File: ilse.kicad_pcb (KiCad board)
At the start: 2 copper layers, 80.9 x 128.5 mm, 89 parts, among them J1 OUT, J2 EURO RACK POWER, J3 CV Inputs, J4 1V/Oct, J5 Gate, J6 Cutoff, J7 Filter In, Q1 BC560, Q2 BC560, Q3 BC560, Q4 BC550, Q5 BC550, Q6 BC550, SW1 Power Switch, SW2 LFO to Filter / Freq CV, SW3 Resonance L/H, U1 TL074, U2 TL074

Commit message: incorporates max's powersupply protection
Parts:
- removed SW1: Power Switch, chair:PVA2
- added D3: 1N5819, Diode_THT:D_DO-41_SOD81_P10.16mm_Horizontal, F.Cu at (46.6, 85.0)
- added D4: 1N5819, Diode_THT:D_DO-41_SOD81_P10.16mm_Horizontal, F.Cu at (46.6, 89.3)
- RV7: value 100kA -> 100kB
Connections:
- C12 pad 1: Net-(BT1-Pad1) -> VCC
- C13 pad 2: Net-(BT2-Pad2) -> VSS
- SW2 pad 4: Net-(SW2-Pad4) -> unconnected-(SW2-Pad4)
- SW3 pad 3: Net-(SW3-Pad3) -> unconnected-(SW3-Pad3)

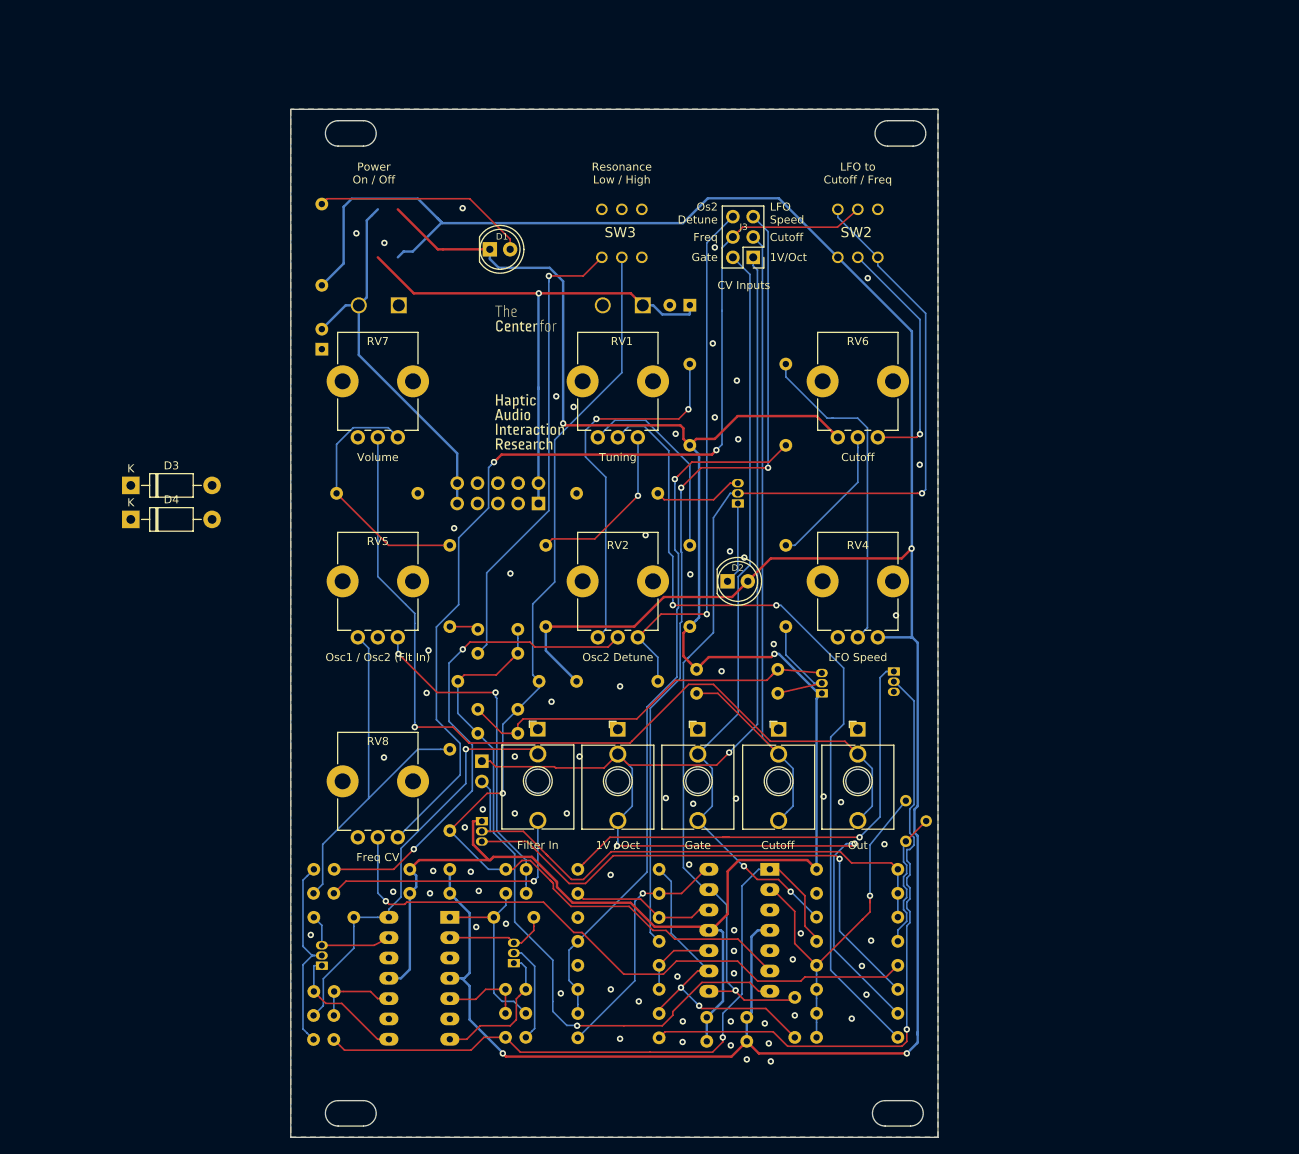
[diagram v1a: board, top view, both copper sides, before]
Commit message: added hybrid lib
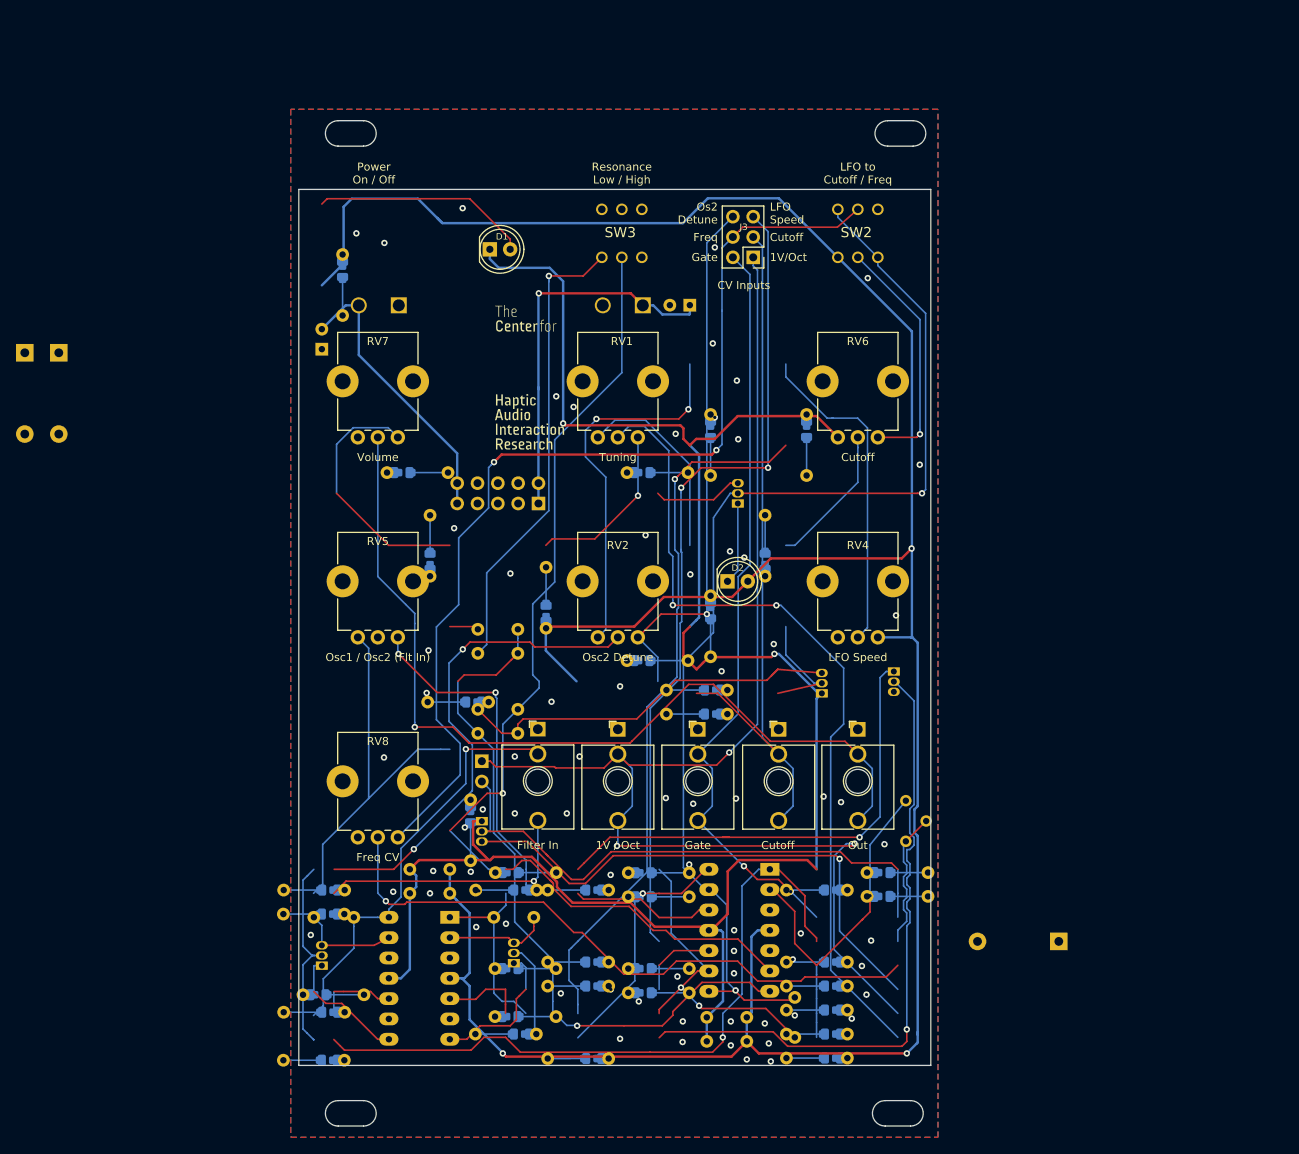
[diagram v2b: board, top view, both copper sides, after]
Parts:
- added D5: 1N5819, Diode_THT:D_DO-41_SOD81_P10.16mm_Horizontal, B.Cu at (162.6, 142.0)
- C8, C9: value 22n -> 47n
- D3, D4: moved to B.Cu
- R1, R12, R15, R19, R2, R20, R21, R23, R27, R28, R29, R3, R30, R31, R32, R33, R34, R35, R36, R37, R38, R39, R4, R40, R7, R8, R9: footprint Resistor_THT:R_Axial_DIN0207_L6.3mm_D2.5mm_P10.16mm_Horizontal -> hybrid:R (hybrid SMD-THT)
- R10, R11, R13, R14, R16, R17, R18, R22, R5, R6: footprint Resistor_THT:R_Axial_DIN0207_L6.3mm_D2.5mm_P2.54mm_Vertical -> hybrid:R (hybrid SMD-THT)
- R24, R25: value 47k -> 100k; footprint Resistor_THT:R_Axial_DIN0207_L6.3mm_D2.5mm_P10.16mm_Horizontal -> hybrid:R (hybrid SMD-THT)
- R26: value 100k -> 10k; footprint Resistor_THT:R_Axial_DIN0207_L6.3mm_D2.5mm_P10.16mm_Horizontal -> hybrid:R (hybrid SMD-THT)
- moved D4 24.7 mm to (33.4, 68.4), turned to -90 degrees
- moved D3 18.9 mm to (37.6, 68.4), turned to -90 degrees
- moved R1 7.02 mm to (101.1, 99.0)
- moved R34 0.12 mm to (86.6, 92.5)
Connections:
- Q5 pad 1: VSS -> GND
- R26 pad 1: VSS -> Net-(C8-Pad2)
- R26 pad 2: Net-(C8-Pad2) -> Net-(Q5-Pad2)
- RV6 pad 1: VSS -> GND
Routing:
- net VSS: track 271.1 -> 843.9 mm, vias 3 -> 11
- net VCC: track 351.4 -> 704.1 mm, vias 3 -> 10
- net 1V/Oct: track 165.8 -> 0.00 mm, vias 3 -> 0
- net Net-(C7-Pad2): track 143.7 -> 0.00 mm, vias 2 -> 0
- net Net-(Q5-Pad2): track 15.1 -> 125.9 mm, vias 0 -> 1
- net Net-(J1-PadT): track 110.8 -> 0.00 mm, vias 1 -> 0
- net LFO Speed: track 103.2 -> 0.00 mm, vias 2 -> 0
- net Net-(R7-Pad2): track 102.6 -> 0.00 mm, vias 2 -> 0
- net Net-(R18-Pad1): track 48.1 -> 143.8 mm, vias 0 -> 3
- net Net-(C8-Pad1): track 131.3 -> 39.9 mm, vias 1 -> 2
- net Net-(R30-Pad1): track 17.9 -> 107.1 mm
- net Filter Cutoff: track 89.2 -> 0.00 mm
- net Net-(R19-Pad1): track 88.7 -> 0.00 mm, vias 1 -> 0
- net Net-(R15-Pad1): track 88.1 -> 0.00 mm
- net Net-(C7-Pad1): track 40.8 -> 117.8 mm, vias 2 -> 3
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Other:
- board size 80.9 x 128.5 mm -> 79 x 109.5 mm

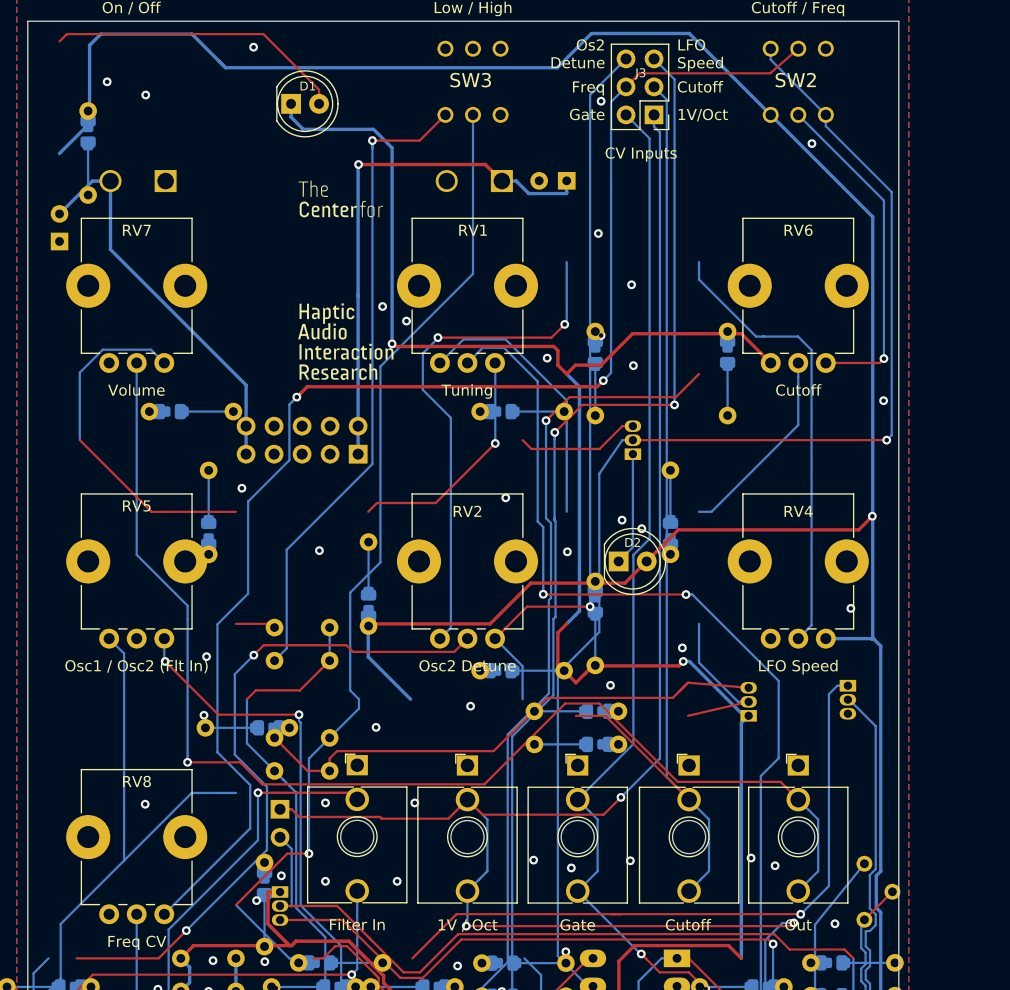
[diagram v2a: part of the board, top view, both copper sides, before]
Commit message: edits in schematic
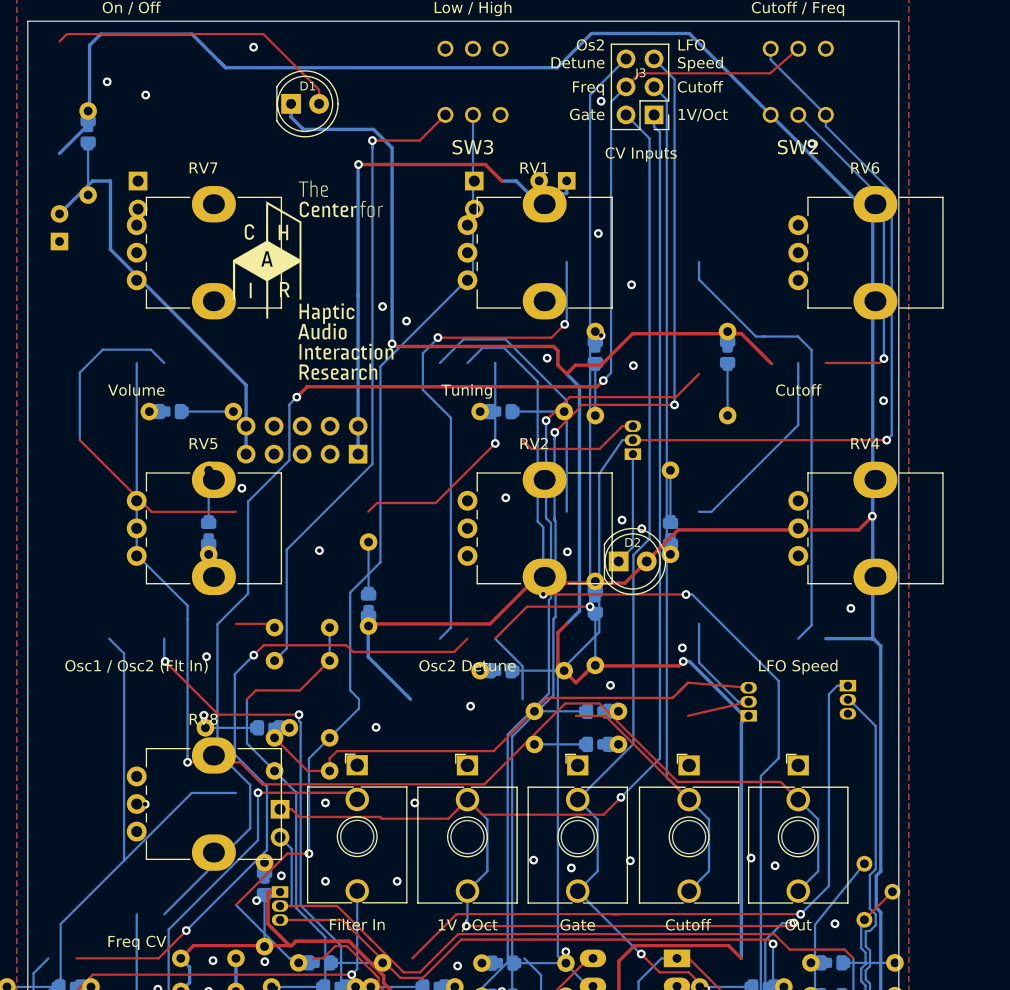
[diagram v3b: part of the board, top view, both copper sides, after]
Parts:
- BT1, BT2: footprint chair:Battery Connector -> Connector_PinHeader_2.54mm:PinHeader_1x02_P2.54mm_Vertical
- J1, J4, J5, J6, J7: footprint chair:Jack_3.5mm_QingPu_WQP-PJ398SM_Vertical_CircularHoles -> CHAIR:Jack_3.5mm_QingPu_WQP-WQP518MA
- J2: footprint 4ms-footprints:Euro_Header_10-pin_TH -> CHAIR:Euro_Header_10-pin_TH
- LOGO1: footprint chair:CHAIR -> CHAIR:CHAIR_logo_silkscreen
- RV1, RV2, RV4, RV5, RV6, RV7, RV8: footprint chair:Potentiometer_Alps_RK09K_Single_Vertical -> CHAIR:Potentiometer_Alps_RK09K_Single_Vertical
- SW2, SW3: footprint chair:PVA2 -> CHAIR:Switch_DPDT_PVA2
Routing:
- net VCC: track 704.1 -> 814.2 mm, vias 10 -> 12
- net Net-(R36-Pad2): track 102.6 -> 0.00 mm, vias 2 -> 1
- net Net-(C8-Pad1): track 39.9 -> 0.00 mm
- net Net-(Q4-Pad1): track 60.8 -> 100.7 mm
- net GND: track 58.9 -> 21.4 mm, vias 66 -> 64
- net GATE: track 95.3 -> 132.8 mm, vias 2 -> 3
- net Net-(R34-Pad1): track 32.0 -> 15.1 mm
- net Net-(Q5-Pad2): track 125.9 -> 142.8 mm
- net Net-(BT1-Pad1): track 47.6 -> 40.1 mm

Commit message: layout remake in process
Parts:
- C1, C10, C11, C2, C3, C4, C5, C6, C7, C8, C9: footprint Capacitor_THT:C_Rect_L7.2mm_W2.5mm_P5.00mm_FKS2_FKP2_MKS2_MKP2 -> hybrid:C_Disc_(hybrid SMD-THT)_P5.00mm-0604
- D3, D4: footprint Diode_THT:D_DO-41_SOD81_P10.16mm_Horizontal -> Diode_THT:D_DO-35_SOD27_P7.62mm_Horizontal
- D5: footprint Diode_THT:D_DO-41_SOD81_P10.16mm_Horizontal -> Diode_THT:D_DO-35_SOD27_P7.62mm_Horizontal; moved to F.Cu
- Q1, Q2, Q3: value BC560 -> BC559
- Q4, Q5, Q6: value BC550 -> BC548
- R7: value 20k -> 22k
- U1, U2: footprint Package_DIP:DIP-14_W7.62mm_Socket_LongPads -> Package_DIP:DIP-14_W7.62mm
- moved D5 105.6 mm to (71.3, 88.9), turned to 0 degrees
- moved D3 92.4 mm to (130.0, 71.5), turned to -135 degrees
- moved D4 92.0 mm to (124.6, 80.6), turned to 45 degrees
- moved R31 78.2 mm to (189.9, 74.8)
- moved C13 65.4 mm to (134.9, 79.3), turned to 135 degrees
- moved R12 60.0 mm to (126.7, 39.0), turned to 180 degrees
- moved BT2 46.2 mm to (121.2, 77.8)
- moved LOGO1 28.1 mm to (117.7, 57.1)
- moved R20 27.3 mm to (137.4, 139.4)
- moved R6 27.3 mm to (94.2, 142.6)
- moved H3 27.3 mm to (167.5, 29.4)
- moved J1 27.3 mm to (162.2, 103.9)
- moved J4 27.3 mm to (132.2, 103.9)
- moved J5 27.3 mm to (142.2, 103.9)
- moved J6 27.3 mm to (152.3, 103.9)
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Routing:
- net VSS: track 843.9 -> 261.7 mm, vias 11 -> 3
- net VCC: track 814.2 -> 301.9 mm, vias 12 -> 8
- net 1V/Oct: track 0.00 -> 425.4 mm, vias 0 -> 7
- net Net-(C7-Pad2): track 0.00 -> 143.7 mm, vias 0 -> 3
- net Net-(Q5-Pad2): track 142.8 -> 15.1 mm, vias 1 -> 2
- net Net-(C4-Pad2): track 82.8 -> 193.9 mm, vias 1 -> 4
- net Net-(J1-PadT): track 0.00 -> 110.8 mm, vias 0 -> 1
- net LFO Speed: track 0.00 -> 103.2 mm, vias 0 -> 2
- net Net-(RV5-Pad1): track 143.8 -> 48.1 mm, vias 3 -> 0
- net Net-(R30-Pad1): track 107.1 -> 17.9 mm
- net Net-(U2-Pad1): track 0.00 -> 88.1 mm
- net Net-(C7-Pad1): track 117.8 -> 40.8 mm
- net Net-(C10-Pad2): track 11.9 -> 89.0 mm
- net Net-(R19-Pad2): track 109.5 -> 37.7 mm, vias 1 -> 0
- net Net-(C8-Pad1): track 0.00 -> 68.7 mm, vias 2 -> 1
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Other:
- board size 79 x 109.5 mm -> 80.9 x 128.5 mm
- board text added: "Designed by CHAIR 2020-2022."
- board text removed: "+12V"
- board text removed: "Designed by CHAIR.AUDIO 2020."

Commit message: layout remake in process
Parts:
- removed H1, H2, H3, H4: MountingHole, 4ms-footprints:Rail-mount-slot
- D5, LOGO1: moved to B.Cu
- SW1: renamed from SW2; footprint CHAIR:Switch_DPDT_PVA2 -> hybrid:Switch_DPDT_(Hybrid Miniature-SubMiniature)
- SW2: renamed from SW3; value Resonance L/H -> Resonance; footprint CHAIR:Switch_DPDT_PVA2 -> hybrid:Switch_DPDT_(Hybrid Miniature-SubMiniature)
- moved D5 83.9 mm to (142.0, 134.1), turned to 180 degrees
- moved R27 66.7 mm to (161.4, 143.0)
- moved R7 59.9 mm to (150.7, 82.8), turned to 180 degrees
- moved R23 55.3 mm to (161.4, 140.0), turned to 0 degrees
- moved Q4 54.2 mm to (128.6, 135.1), turned to 90 degrees
- moved R16 51.4 mm to (169.0, 124.7)
- moved R32 50.3 mm to (150.7, 85.9), turned to 180 degrees
- moved R38 45.5 mm to (121.7, 124.5), turned to 0 degrees
- moved C9 42.8 mm to (149.4, 73.4)
- moved C8 39.6 mm to (144.4, 70.4), turned to 0 degrees
- moved R31 39.5 mm to (150.7, 79.5)
- moved R33 38.0 mm to (166.2, 70.0), turned to -90 degrees
- moved R37 35.9 mm to (143.1, 100.8), turned to 0 degrees
- moved R4 35.0 mm to (128.3, 100.8), turned to 0 degrees
- moved C10 34.2 mm to (114.4, 60.2)
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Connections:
- SW1 pad 4: unconnected-(SW2-Pad4) -> Net-(C7-Pad2)
- SW1 pad 6: Net-(C7-Pad2) -> unconnected-(SW1-Pad6)
- SW2 pad 4: (no net) -> Net-(C10-Pad1)
- SW2 pad 5: (no net) -> Net-(C8-Pad1)
- SW2 pad 6: (no net) -> unconnected-(SW2-Pad6)
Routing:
- net 1V/Oct: track 425.4 -> 0.00 mm, vias 7 -> 0
- net VCC: track 301.9 -> 11.2 mm, vias 8 -> 0
- net VSS: track 261.7 -> 9.64 mm, vias 3 -> 0
- net Net-(C4-Pad2): track 193.9 -> 0.00 mm, vias 4 -> 0
- net Net-(C7-Pad2): track 143.7 -> 8.74 mm, vias 3 -> 0
- net Net-(J1-PadT): track 110.8 -> 0.00 mm, vias 1 -> 0
- net LFO Speed: track 103.2 -> 0.00 mm, vias 2 -> 0
- net Net-(C10-Pad2): track 89.0 -> 0.00 mm, vias 1 -> 0
- net GND: track 88.7 -> 0.00 mm, vias 52 -> 2
- net Net-(R15-Pad1): track 88.1 -> 0.00 mm, vias 1 -> 0
- net GATE: track 95.3 -> 11.0 mm, vias 2 -> 0
- net Net-(Q4-Pad2): track 80.4 -> 0.00 mm, vias 2 -> 0
- net Freq CV: track 80.0 -> 0.00 mm, vias 1 -> 0
- net Net-(C8-Pad1): track 68.7 -> 0.00 mm, vias 1 -> 0
- net Osc 2 Detune: track 67.4 -> 0.00 mm, vias 1 -> 0
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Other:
- board size 80.9 x 128.5 mm -> 81 x 109.5 mm
- board text added: "LFO to Freq / Cutoff"
- board text removed: "GND"
- board text removed: "LFO to Cutoff / Freq"
- board text removed: "Power On / Off"
